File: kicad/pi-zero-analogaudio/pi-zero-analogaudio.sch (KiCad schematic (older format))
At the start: 10 parts, among them J1 AudioJack3, J2 Female Connector 2x5

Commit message: Revision 3: added connector for audio-out
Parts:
- added J3: Audio-Out, symbol Connector:Conn_01x02_Male
- J2: value Female Connector 2x5 -> Pi Connector 2x5 Female
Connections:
- wire segments 28 -> 32
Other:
- note added: "Left\nRight"
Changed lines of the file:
@@
 Title "Pi-Zero Analog Audio"
 Date "2019-12-22"
-Rev "2"
+Rev "3"
 Comp "Bernhard Bablok"
 Comment1 ""
@@
 Connection ~ 4850 1900
 Wire Wire Line
-	4850 2150 5850 2150
+	4850 2150 5500 2150
 Wire Wire Line
 	5850 2150 5850 2100
 Connection ~ 4850 2150
-Wire Wire Line
-	4850 1500 5850 1500
 Connection ~ 4850 1500
 Wire Wire Line
@@
 P 1800 1850
 F 0 "J2" H 1850 2267 50  0000 C CNN
-F 1 "Female Connector 2x5" H 1850 2176 50  0000 C CNN
+F 1 "Pi Connector 2x5 Female" H 1850 2176 50  0000 C CNN
 F 2 "" H 1800 1850 50  0001 C CNN
 F 3 "~" H 1800 1850 50  0001 C CNN
@@
 NoConn ~ 2100 1850
 NoConn ~ 2100 2050
+Wire Wire Line
+	4850 1500 5850 1500
+$Comp
+L Connector:Conn_01x02_Male J3
+U 1 1 5E060129
+P 6200 1600
+F 0 "J3" H 6172 1482 50  0000 R CNN
+F 1 "Audio-Out" H 6172 1573 50  0000 R CNN
+F 2 "" H 6200 1600 50  0001 C CNN
+F 3 "~" H 6200 1600 50  0001 C CNN
+	1    6200 1600
+	-1   0    0    1
+$EndComp
+Wire Wire Line
+	5850 1500 6000 1500
+Connection ~ 5850 1500
+Wire Wire Line
+	5500 2150 5500 1600
+Wire Wire Line
+	5500 1600 6000 1600
+Connection ~ 5500 2150
+Wire Wire Line
+	5500 2150 5850 2150
+Text Notes 6700 1600 0    50   ~ 0
+Left\nRight
 $EndSCHEMATC

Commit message: added footprints and started pcb
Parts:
- C1, C3: footprint (none) -> Capacitor_THT:C_Disc_D3.0mm_W1.6mm_P2.50mm
- C2, C4: footprint (none) -> Capacitor_THT:CP_Radial_D4.0mm_P1.50mm
- J1: footprint (none) -> Connector_Audio:Jack_3.5mm_Ledino_KB3SPRS_Horizontal
- J2: footprint (none) -> Connector_PinSocket_2.54mm:PinSocket_2x05_P2.54mm_Vertical
- J3: footprint (none) -> Connector_PinHeader_2.54mm:PinHeader_1x02_P2.54mm_Vertical
- R1, R2, R3, R4: footprint (none) -> Resistor_THT:R_Axial_DIN0207_L6.3mm_D2.5mm_P7.62mm_Horizontal
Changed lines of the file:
@@
 F 0 "R1" V 3293 1500 50  0000 C CNN
 F 1 "270 Ohm" V 3384 1500 50  0000 C CNN
-F 2 "" V 3430 1500 50  0001 C CNN
+F 2 "Resistor_THT:R_Axial_DIN0207_L6.3mm_D2.5mm_P7.62mm_Horizontal" V 3430 1500 50  0001 C CNN
 F 3 "~" H 3500 1500 50  0001 C CNN
 	1    3500 1500
@@
 F 0 "R2" H 4920 1796 50  0000 L CNN
 F 1 "150 Ohm" H 4920 1705 50  0000 L CNN
-F 2 "" V 4780 1750 50  0001 C CNN
+F 2 "Resistor_THT:R_Axial_DIN0207_L6.3mm_D2.5mm_P7.62mm_Horizontal" V 4780 1750 50  0001 C CNN
 F 3 "~" H 4850 1750 50  0001 C CNN
 	1    4850 1750
@@
 F 0 "C1" H 4215 1796 50  0000 L CNN
 F 1 "33 nF" H 4215 1705 50  0000 L CNN
-F 2 "" H 4138 1600 50  0001 C CNN
+F 2 "Capacitor_THT:C_Disc_D3.0mm_W1.6mm_P2.50mm" H 4138 1600 50  0001 C CNN
 F 3 "~" H 4100 1750 50  0001 C CNN
 	1    4100 1750
@@
 F 0 "C2" V 4752 1500 50  0000 C CNN
 F 1 "10 µF" V 4661 1500 50  0000 C CNN
-F 2 "" H 4500 1500 50  0001 C CNN
+F 2 "Capacitor_THT:CP_Radial_D4.0mm_P1.50mm" H 4500 1500 50  0001 C CNN
 F 3 "~" H 4500 1500 50  0001 C CNN
 	1    4500 1500
@@
 F 0 "R3" V 3293 2550 50  0000 C CNN
 F 1 "270 Ohm" V 3384 2550 50  0000 C CNN
-F 2 "" V 3430 2550 50  0001 C CNN
+F 2 "Resistor_THT:R_Axial_DIN0207_L6.3mm_D2.5mm_P7.62mm_Horizontal" V 3430 2550 50  0001 C CNN
 F 3 "~" H 3500 2550 50  0001 C CNN
 	1    3500 2550
@@
 F 0 "R4" H 4920 2346 50  0000 L CNN
 F 1 "150 Ohm" H 4920 2255 50  0000 L CNN
-F 2 "" V 4780 2300 50  0001 C CNN
+F 2 "Resistor_THT:R_Axial_DIN0207_L6.3mm_D2.5mm_P7.62mm_Horizontal" V 4780 2300 50  0001 C CNN
 F 3 "~" H 4850 2300 50  0001 C CNN
 	1    4850 2300
@@
 F 0 "C3" H 4215 2346 50  0000 L CNN
 F 1 "33 nF" H 4215 2255 50  0000 L CNN
-F 2 "" H 4138 2150 50  0001 C CNN
+F 2 "Capacitor_THT:C_Disc_D3.0mm_W1.6mm_P2.50mm" H 4138 2150 50  0001 C CNN
 F 3 "~" H 4100 2300 50  0001 C CNN
 	1    4100 2300
@@
 F 0 "C4" V 4752 2550 50  0000 C CNN
 F 1 "10 µF" V 4661 2550 50  0000 C CNN
-F 2 "" H 4500 2550 50  0001 C CNN
+F 2 "Capacitor_THT:CP_Radial_D4.0mm_P1.50mm" H 4500 2550 50  0001 C CNN
 F 3 "~" H 4500 2550 50  0001 C CNN
 	1    4500 2550
@@
 F 0 "J1" H 5770 2025 50  0000 R CNN
 F 1 "AudioJack3" H 5770 1934 50  0000 R CNN
-F 2 "" H 6050 2000 50  0001 C CNN
+F 2 "Connector_Audio:Jack_3.5mm_Ledino_KB3SPRS_Horizontal" H 6050 2000 50  0001 C CNN
 F 3 "~" H 6050 2000 50  0001 C CNN
 	1    6050 2000
@@
 F 0 "J2" H 1850 2267 50  0000 C CNN
 F 1 "Pi Connector 2x5 Female" H 1850 2176 50  0000 C CNN
-F 2 "" H 1800 1850 50  0001 C CNN
+F 2 "Connector_PinSocket_2.54mm:PinSocket_2x05_P2.54mm_Vertical" H 1800 1850 50  0001 C CNN
 F 3 "~" H 1800 1850 50  0001 C CNN
 	1    1800 1850
@@
 F 0 "J3" H 6172 1482 50  0000 R CNN
 F 1 "Audio-Out" H 6172 1573 50  0000 R CNN
-F 2 "" H 6200 1600 50  0001 C CNN
+F 2 "Connector_PinHeader_2.54mm:PinHeader_1x02_P2.54mm_Vertical" H 6200 1600 50  0001 C CNN
 F 3 "~" H 6200 1600 50  0001 C CNN
 	1    6200 1600

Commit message: fixed wrong connection for R4
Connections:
- wire segments 32 -> 33
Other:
- note added: "Right\nLeft"
- note removed: "Left\nRight"
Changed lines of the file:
@@
 Title "Pi-Zero Analog Audio"
 Date "2019-12-22"
-Rev "3"
+Rev "4"
 Comp "Bernhard Bablok"
 Comment1 ""
@@
 Connection ~ 4850 1900
 Wire Wire Line
-	4850 2150 5500 2150
-Wire Wire Line
 	5850 2150 5850 2100
-Connection ~ 4850 2150
 Connection ~ 4850 1500
 Wire Wire Line
@@
 Wire Wire Line
 	5500 1600 6000 1600
-Connection ~ 5500 2150
 Wire Wire Line
 	5500 2150 5850 2150
 Text Notes 6700 1600 0    50   ~ 0
-Left\nRight
+Right\nLeft
+Wire Wire Line
+	4850 2550 5500 2550
+Wire Wire Line
+	5500 2550 5500 2150
+Connection ~ 4850 2550
+Connection ~ 5500 2150
 $EndSCHEMATC

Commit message: Revision 5: J3 with additional GND, connect pin34 with pin39
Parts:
- removed J3: Audio-Out, Connector_PinHeader_2.54mm:PinHeader_1x02_P2.54mm_Vertical, symbol Connector:Conn_01x02_Male
- added J3: Audio Out, Connector_PinHeader_2.54mm:PinHeader_1x03_P2.54mm_Vertical, symbol Connector:Conn_01x03_Male
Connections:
- wire segments 33 -> 43
- no-connect marks 7 -> 6
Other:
- note added: "Right\n\nLeft"
- note removed: "Right\nLeft"
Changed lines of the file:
@@
 Sheet 1 1
 Title "Pi-Zero Analog Audio"
-Date "2019-12-22"
-Rev "4"
+Date "2020-01-04"
+Rev "5"
 Comp "Bernhard Bablok"
 Comment1 ""
@@
 $EndComp
 Wire Wire Line
-	4850 1900 5850 1900
+	4850 1900 5350 1900
 Connection ~ 4850 1900
 Wire Wire Line
 	5850 2150 5850 2100
 Connection ~ 4850 1500
-Wire Wire Line
-	5850 1500 5850 2000
 $Comp
 L Connector_Generic:Conn_02x05_Odd_Even J2
@@
 NoConn ~ 1600 1750
 NoConn ~ 1600 1850
-NoConn ~ 1600 1950
 NoConn ~ 2100 1750
 NoConn ~ 2100 1850
@@
 Wire Wire Line
 	4850 1500 5850 1500
-$Comp
-L Connector:Conn_01x02_Male J3
-U 1 1 5E060129
-P 6200 1600
-F 0 "J3" H 6172 1482 50  0000 R CNN
-F 1 "Audio-Out" H 6172 1573 50  0000 R CNN
-F 2 "Connector_PinHeader_2.54mm:PinHeader_1x02_P2.54mm_Vertical" H 6200 1600 50  0001 C CNN
-F 3 "~" H 6200 1600 50  0001 C CNN
-	1    6200 1600
-	-1   0    0    1
-$EndComp
-Wire Wire Line
-	5850 1500 6000 1500
-Connection ~ 5850 1500
-Wire Wire Line
-	5500 2150 5500 1600
-Wire Wire Line
-	5500 1600 6000 1600
 Wire Wire Line
 	5500 2150 5850 2150
-Text Notes 6700 1600 0    50   ~ 0
-Right\nLeft
+Text Notes 6750 1700 0    50   ~ 0
+Right\n\nLeft
 Wire Wire Line
 	4850 2550 5500 2550
@@
 	5500 2550 5500 2150
 Connection ~ 4850 2550
+$Comp
+L Connector:Conn_01x03_Male J3
+U 1 1 5E107AFE
+P 6350 1600
+F 0 "J3" H 6322 1532 50  0000 R CNN
+F 1 "Audio Out" H 6322 1623 50  0000 R CNN
+F 2 "Connector_PinHeader_2.54mm:PinHeader_1x03_P2.54mm_Vertical" H 6350 1600 50  0001 C CNN
+F 3 "~" H 6350 1600 50  0001 C CNN
+	1    6350 1600
+	-1   0    0    1
+$EndComp
+Wire Wire Line
+	5850 1500 5850 2000
+Wire Wire Line
+	5500 2150 5500 1700
+Wire Wire Line
+	5500 1700 6150 1700
 Connection ~ 5500 2150
+Wire Wire Line
+	5850 1500 6150 1500
+Connection ~ 5850 1500
+Wire Wire Line
+	6150 1600 5350 1600
+Wire Wire Line
+	5350 1600 5350 1900
+Connection ~ 5350 1900
+Wire Wire Line
+	5350 1900 5850 1900
+Wire Wire Line
+	1600 1950 750  1950
+Wire Wire Line
+	1900 1650 1950 1650
+Wire Wire Line
+	1950 1650 1950 1300
+Wire Wire Line
+	1950 1300 750  1300
+Wire Wire Line
+	750  1300 750  1950
+Connection ~ 750  1950
+Wire Wire Line
+	750  2150 750  1950
+Connection ~ 3200 2150
+Wire Wire Line
+	3200 2150 750  2150
 $EndSCHEMATC

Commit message: added GND/PWR_FLAG
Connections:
- net at C1.2, C3.2, J1.S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: no longer J2.7 (Pin_7), J3.2 (Pin_2)
- new net GND: J2.7 (Pin_7), J3.2 (Pin_2)
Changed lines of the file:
@@
 Title "Pi-Zero Analog Audio"
 Date "2020-01-04"
-Rev "5"
+Rev "6"
 Comp "Bernhard Bablok"
 Comment1 ""
@@
 	-1   0    0    -1
 $EndComp
-Wire Wire Line
-	4850 1900 5350 1900
 Connection ~ 4850 1900
 Wire Wire Line
@@
 Connection ~ 5850 1500
 Wire Wire Line
-	6150 1600 5350 1600
-Wire Wire Line
-	5350 1600 5350 1900
-Connection ~ 5350 1900
-Wire Wire Line
-	5350 1900 5850 1900
-Wire Wire Line
 	1600 1950 750  1950
 Wire Wire Line
@@
 	1950 1650 1950 1300
 Wire Wire Line
-	1950 1300 750  1300
+	1950 1300 1300 1300
 Wire Wire Line
 	750  1300 750  1950
-Connection ~ 750  1950
-Wire Wire Line
-	750  2150 750  1950
-Connection ~ 3200 2150
-Wire Wire Line
-	3200 2150 750  2150
+$Comp
+L power:GND #PWR0101
+U 1 1 5E145812
+P 1300 1050
+F 0 "#PWR0101" H 1300 800 50  0001 C CNN
+F 1 "GND" H 1305 877 50  0000 C CNN
+F 2 "" H 1300 1050 50  0001 C CNN
+F 3 "" H 1300 1050 50  0001 C CNN
+	1    1300 1050
+	-1   0    0    1
+$EndComp
+Wire Wire Line
+	1300 1050 1300 1150
+Connection ~ 1300 1300
+Wire Wire Line
+	1300 1300 750  1300
+$Comp
+L power:PWR_FLAG #FLG0101
+U 1 1 5E147CAD
+P 1700 1050
+F 0 "#FLG0101" H 1700 1125 50  0001 C CNN
+F 1 "PWR_FLAG" H 1700 1223 50  0000 C CNN
+F 2 "" H 1700 1050 50  0001 C CNN
+F 3 "~" H 1700 1050 50  0001 C CNN
+	1    1700 1050
+	1    0    0    -1
+$EndComp
+Wire Wire Line
+	1300 1150 1700 1150
+Wire Wire Line
+	1700 1150 1700 1050
+Connection ~ 1300 1150
+Wire Wire Line
+	1300 1150 1300 1300
+Wire Wire Line
+	4850 1900 5850 1900
+$Comp
+L power:GND #PWR0102
+U 1 1 5E149127
+P 5500 1100
+F 0 "#PWR0102" H 5500 850 50  0001 C CNN
+F 1 "GND" H 5505 927 50  0000 C CNN
+F 2 "" H 5500 1100 50  0001 C CNN
+F 3 "" H 5500 1100 50  0001 C CNN
+	1    5500 1100
+	-1   0    0    1
+$EndComp
+Wire Wire Line
+	6150 1600 5500 1600
+Wire Wire Line
+	5500 1600 5500 1100
 $EndSCHEMATC

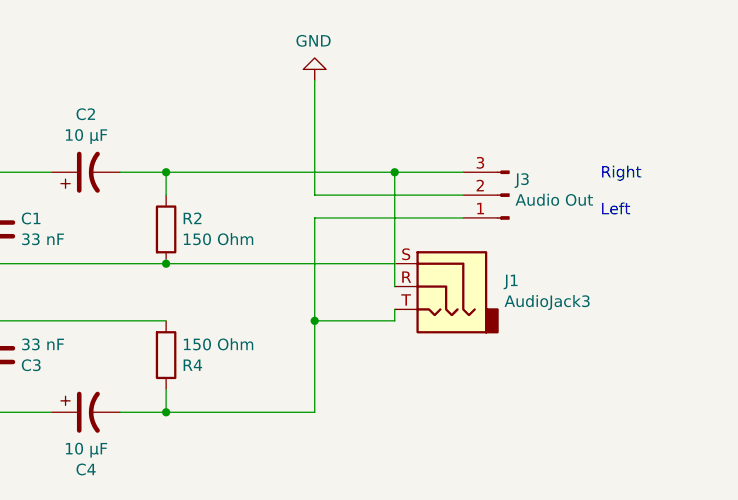
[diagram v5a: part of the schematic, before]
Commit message: Revision 6: replace generic audio-jack with STX-3120-3B
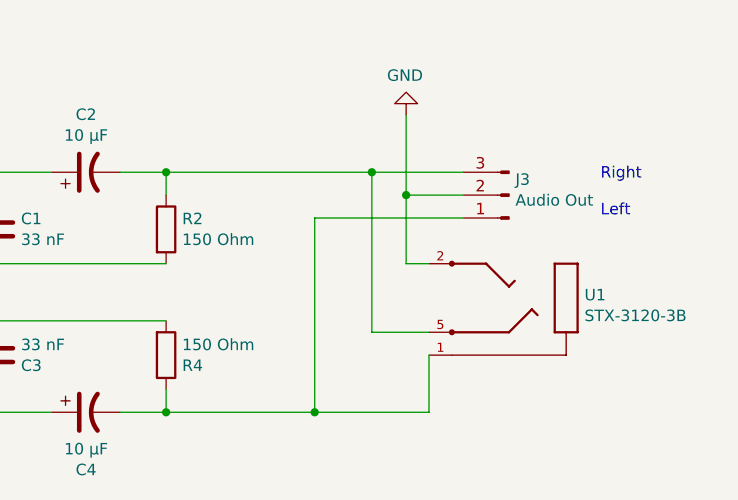
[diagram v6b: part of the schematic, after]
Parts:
- removed J1: AudioJack3, Connector_Audio:Jack_3.5mm_Ledino_KB3SPRS_Horizontal, symbol Connector:AudioJack3
- added U1: STX-3120-3B, STX-3120, symbol STX-3120-3B:STX-3120-3B
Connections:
- net GND: now also U1.2
- net at C2.2, J3.3 (Pin_3), R2.1: now also U1.5
- net at C4.2, J3.1 (Pin_1), R4.1: now also U1.1
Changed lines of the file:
@@
 Wire Wire Line
 	3200 2150 3200 1900
-$Comp
-L Connector:AudioJack3 J1
-U 1 1 5E012848
-P 6050 2000
-F 0 "J1" H 5770 2025 50  0000 R CNN
-F 1 "AudioJack3" H 5770 1934 50  0000 R CNN
-F 2 "Connector_Audio:Jack_3.5mm_Ledino_KB3SPRS_Horizontal" H 6050 2000 50  0001 C CNN
-F 3 "~" H 6050 2000 50  0001 C CNN
-	1    6050 2000
-	-1   0    0    -1
-$EndComp
-Connection ~ 4850 1900
-Wire Wire Line
-	5850 2150 5850 2100
 Connection ~ 4850 1500
 $Comp
@@
 NoConn ~ 2100 1850
 NoConn ~ 2100 2050
-Wire Wire Line
-	4850 1500 5850 1500
-Wire Wire Line
-	5500 2150 5850 2150
 Text Notes 6750 1700 0    50   ~ 0
 Right\n\nLeft
 Wire Wire Line
 	4850 2550 5500 2550
-Wire Wire Line
-	5500 2550 5500 2150
 Connection ~ 4850 2550
 $Comp
@@
 $EndComp
 Wire Wire Line
-	5850 1500 5850 2000
-Wire Wire Line
-	5500 2150 5500 1700
-Wire Wire Line
 	5500 1700 6150 1700
-Connection ~ 5500 2150
-Wire Wire Line
-	5850 1500 6150 1500
-Connection ~ 5850 1500
 Wire Wire Line
 	1600 1950 750  1950
@@
 Wire Wire Line
 	1300 1150 1300 1300
-Wire Wire Line
-	4850 1900 5850 1900
 $Comp
-L power:GND #PWR0102
-U 1 1 5E149127
-P 5500 1100
-F 0 "#PWR0102" H 5500 850 50  0001 C CNN
-F 1 "GND" H 5505 927 50  0000 C CNN
-F 2 "" H 5500 1100 50  0001 C CNN
-F 3 "" H 5500 1100 50  0001 C CNN
-	1    5500 1100
+L STX-3120-3B:STX-3120-3B U1
+U 1 1 5E14E2BF
+P 6200 2200
+F 0 "U1" H 5720 2037 50  0000 R CNN
+F 1 "STX-3120-3B" H 5720 2128 50  0000 R CNN
+F 2 "STX-3120" H 6200 2200 50  0001 L BNN
+F 3 "" H 6200 2200 50  0001 C CNN
+	1    6200 2200
 	-1   0    0    1
 $EndComp
 Wire Wire Line
-	6150 1600 5500 1600
+	5500 1700 5500 2550
 Wire Wire Line
-	5500 1600 5500 1100
+	4850 1500 5750 1500
+Wire Wire Line
+	5500 2550 6000 2550
+Wire Wire Line
+	6000 2550 6000 2300
+Connection ~ 5500 2550
+Wire Wire Line
+	6000 2200 5750 2200
+Wire Wire Line
+	5750 2200 5750 1500
+Connection ~ 5750 1500
+Wire Wire Line
+	5750 1500 6150 1500
+$Comp
+L power:GND #PWR?
+U 1 1 5E153B4C
+P 5900 1250
+F 0 "#PWR?" H 5900 1000 50  0001 C CNN
+F 1 "GND" H 5905 1077 50  0000 C CNN
+F 2 "" H 5900 1250 50  0001 C CNN
+F 3 "" H 5900 1250 50  0001 C CNN
+	1    5900 1250
+	-1   0    0    1
+$EndComp
+Wire Wire Line
+	6150 1600 5900 1600
+Wire Wire Line
+	5900 1600 5900 1250
+Wire Wire Line
+	6000 1900 5900 1900
+Wire Wire Line
+	5900 1900 5900 1600
+Connection ~ 5900 1600
 $EndSCHEMATC

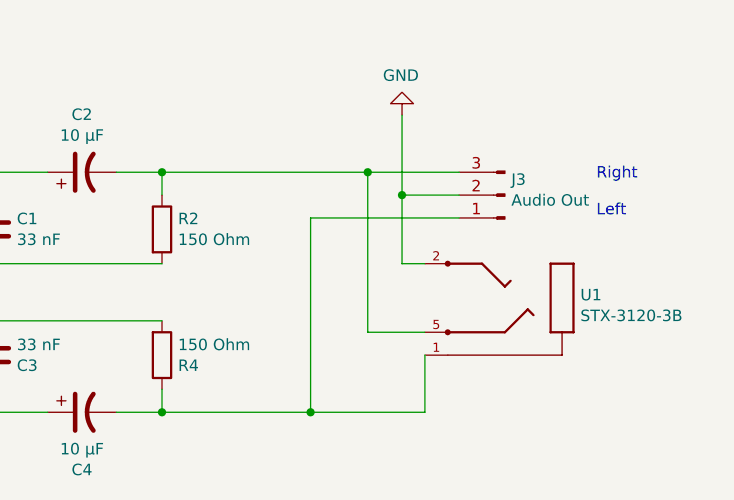
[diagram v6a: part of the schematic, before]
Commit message: updated layout (size, components)
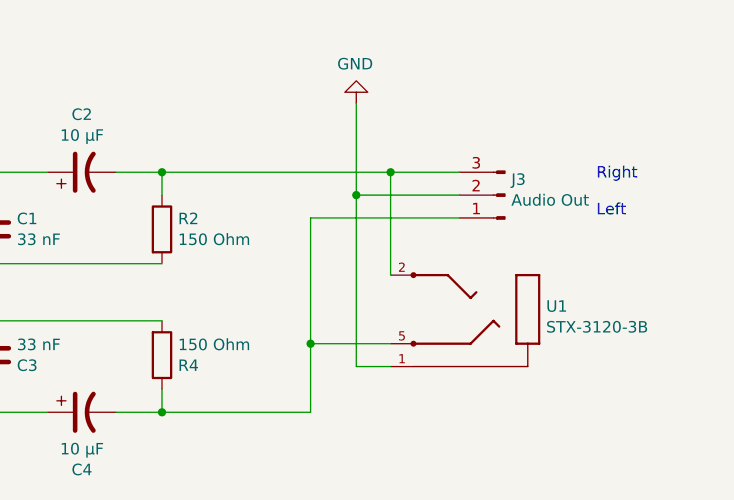
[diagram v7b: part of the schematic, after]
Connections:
- net GND: now also U1.1; no longer U1.2
- net at C2.2, J3.3 (Pin_3), R2.1: now also U1.2; no longer U1.5
- net at C4.2, J3.1 (Pin_1), R4.1: now also U1.5; no longer U1.1
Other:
- moved on the sheet: U1
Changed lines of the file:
@@
 Wire Wire Line
 	1300 1150 1300 1300
+Wire Wire Line
+	5500 1700 5500 2250
 $Comp
 L STX-3120-3B:STX-3120-3B U1
 U 1 1 5E14E2BF
-P 6200 2200
-F 0 "U1" H 5720 2037 50  0000 R CNN
-F 1 "STX-3120-3B" H 5720 2128 50  0000 R CNN
-F 2 "STX-3120" H 6200 2200 50  0001 L BNN
-F 3 "" H 6200 2200 50  0001 C CNN
-	1    6200 2200
+P 6050 2250
+F 0 "U1" H 5570 2087 50  0000 R CNN
+F 1 "STX-3120-3B" H 5570 2178 50  0000 R CNN
+F 2 "STX-3120" H 6050 2250 50  0001 L BNN
+F 3 "" H 6050 2250 50  0001 C CNN
+	1    6050 2250
 	-1   0    0    1
 $EndComp
 Wire Wire Line
-	5500 1700 5500 2550
-Wire Wire Line
-	4850 1500 5750 1500
-Wire Wire Line
-	5500 2550 6000 2550
-Wire Wire Line
-	6000 2550 6000 2300
-Connection ~ 5500 2550
-Wire Wire Line
-	6000 2200 5750 2200
-Wire Wire Line
-	5750 2200 5750 1500
-Connection ~ 5750 1500
-Wire Wire Line
-	5750 1500 6150 1500
+	4850 1500 5850 1500
 $Comp
-L power:GND #PWR?
-U 1 1 5E153B4C
-P 5900 1250
-F 0 "#PWR?" H 5900 1000 50  0001 C CNN
-F 1 "GND" H 5905 1077 50  0000 C CNN
-F 2 "" H 5900 1250 50  0001 C CNN
-F 3 "" H 5900 1250 50  0001 C CNN
-	1    5900 1250
+L power:GND #PWR0102
+U 1 1 5E15C9EB
+P 5700 1200
+F 0 "#PWR0102" H 5700 950 50  0001 C CNN
+F 1 "GND" H 5705 1027 50  0000 C CNN
+F 2 "" H 5700 1200 50  0001 C CNN
+F 3 "" H 5700 1200 50  0001 C CNN
+	1    5700 1200
 	-1   0    0    1
 $EndComp
 Wire Wire Line
-	6150 1600 5900 1600
+	5850 2350 5700 2350
 Wire Wire Line
-	5900 1600 5900 1250
+	5700 2350 5700 1600
 Wire Wire Line
-	6000 1900 5900 1900
+	5700 1600 6150 1600
+Connection ~ 5700 1600
 Wire Wire Line
-	5900 1900 5900 1600
-Connection ~ 5900 1600
+	5700 1600 5700 1200
+Wire Wire Line
+	5850 2250 5500 2250
+Connection ~ 5500 2250
+Wire Wire Line
+	5500 2250 5500 2550
+Wire Wire Line
+	5850 1950 5850 1500
+Connection ~ 5850 1500
+Wire Wire Line
+	5850 1500 6150 1500
 $EndSCHEMATC

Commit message: drilling holes, silk-screen print
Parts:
- added H1, H2: MountingHole, MountingHole:MountingHole_2.7mm_M2.5_DIN965, symbol Mechanical:MountingHole
- U1: footprint STX-3120 -> Download:STX-3120
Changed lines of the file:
@@
 F 0 "U1" H 5570 2087 50  0000 R CNN
 F 1 "STX-3120-3B" H 5570 2178 50  0000 R CNN
-F 2 "STX-3120" H 6050 2250 50  0001 L BNN
+F 2 "Download:STX-3120" H 6050 2250 50  0001 L BNN
 F 3 "" H 6050 2250 50  0001 C CNN
 	1    6050 2250
@@
 Wire Wire Line
 	5850 1500 6150 1500
+$Comp
+L Mechanical:MountingHole H1
+U 1 1 5E161BC7
+P 1400 6800
+F 0 "H1" H 1500 6846 50  0000 L CNN
+F 1 "MountingHole" H 1500 6755 50  0000 L CNN
+F 2 "MountingHole:MountingHole_2.7mm_M2.5_DIN965" H 1400 6800 50  0001 C CNN
+F 3 "~" H 1400 6800 50  0001 C CNN
+	1    1400 6800
+	1    0    0    -1
+$EndComp
+$Comp
+L Mechanical:MountingHole H2
+U 1 1 5E162474
+P 1400 7100
+F 0 "H2" H 1500 7146 50  0000 L CNN
+F 1 "MountingHole" H 1500 7055 50  0000 L CNN
+F 2 "MountingHole:MountingHole_2.7mm_M2.5_DIN965" H 1400 7100 50  0001 C CNN
+F 3 "~" H 1400 7100 50  0001 C CNN
+	1    1400 7100
+	1    0    0    -1
+$EndComp
 $EndSCHEMATC
